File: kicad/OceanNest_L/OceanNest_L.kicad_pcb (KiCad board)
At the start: 2 copper layers, 104.5 x 86 mm, 38 parts, among them J1 MJ-4PP-9_BL_kai, SW1 SW_PUSH, SW10 SW_PUSH, SW11 SW_PUSH, SW12 SW_PUSH, SW13 SW_PUSH, SW14 SW_PUSH, SW15 SW_PUSH, SW16 SW_PUSH, SW2 SW_PUSH, SW3 SW_PUSH, SW4 SW_PUSH, SW5 SW_PUSH, SW6 SW_PUSH, SW7 SW_PUSH, SW8 SW_PUSH, SW9 SW_PUSH, U1 RP2040-Zero

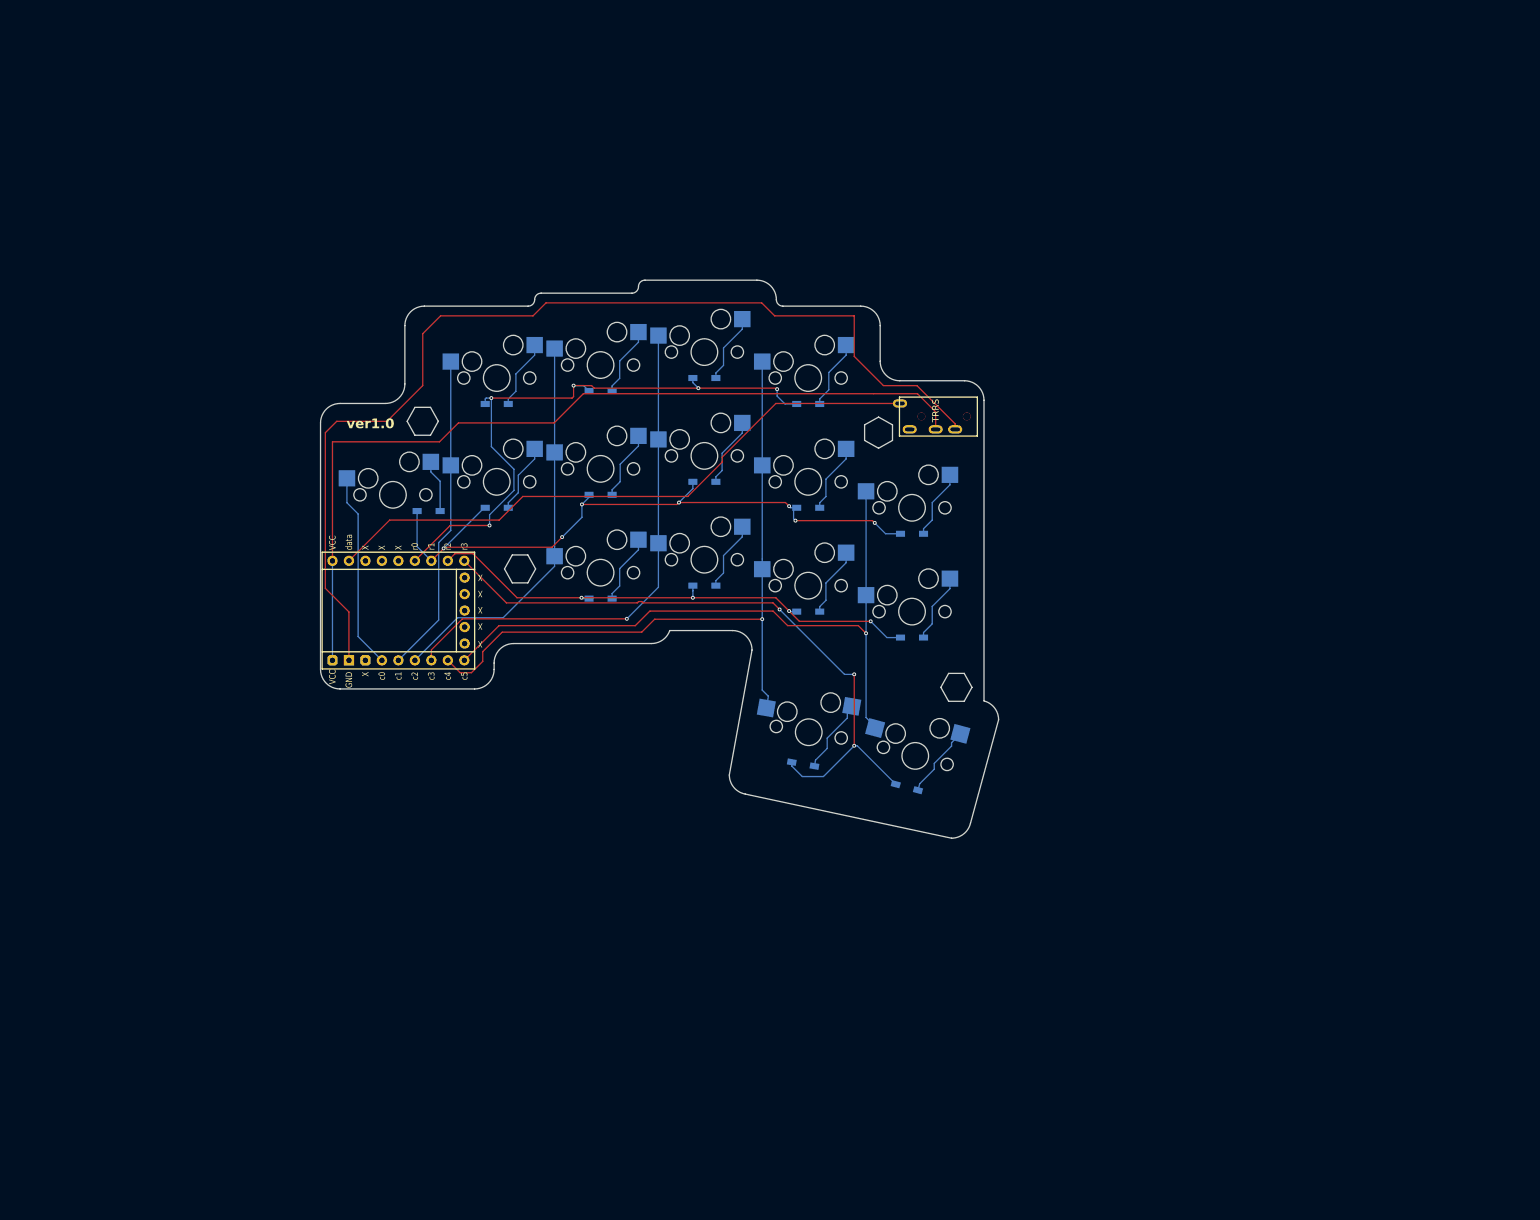
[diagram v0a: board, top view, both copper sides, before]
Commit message: feat: update PCB and schematic files for OceanNest project, including new components and layout adjustments
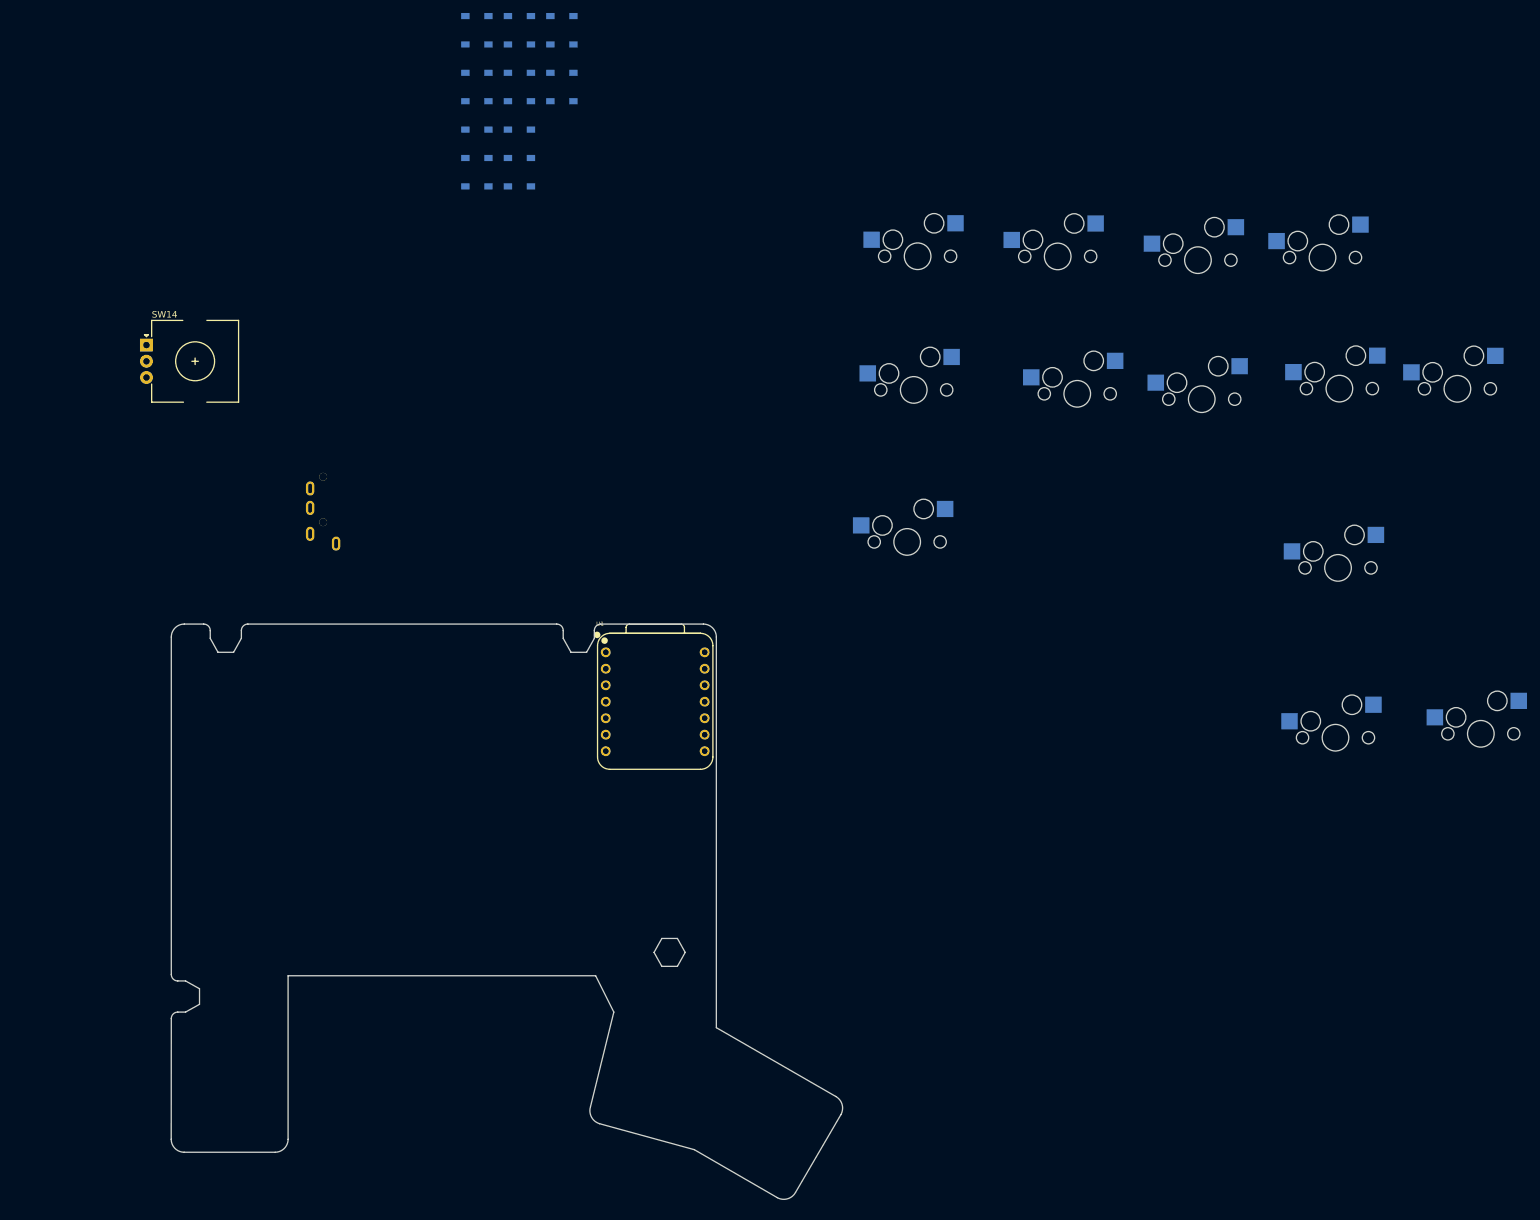
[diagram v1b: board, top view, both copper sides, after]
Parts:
- removed the Ref** at (181.0, 109.8)
- removed the Ref** at (169.0, 70.5)
- removed the Ref** at (113.8, 91.5)
- removed the Ref** at (98.8, 68.8)
- removed SW15, SW16: SW_PUSH, takashicompany:CherryMX_Hotswap_16m
- added D17: D, kbd_Parts:Diode_SMD, F.Cu at (120.2, 15.0)
- added D18: D, kbd_Parts:Diode_SMD, F.Cu at (120.2, 19.4)
- added Ref**: Val**, kbd_Hole:m2_Spacer_Hole_hex, F.Cu at (136.8, 150.6)
- D1, D10, D11, D12, D13, D14, D15, D16, D2, D3, D4, D5, D6, D7, D8, D9: footprint isw-kbd:Diode_SMD -> kbd_Parts:Diode_SMD
- J1: value MJ-4PP-9_BL_kai -> TRRS_MJ-4PP-9; moved to F.Cu
- SW1, SW10, SW11, SW12, SW13, SW2, SW3, SW4, SW5, SW6, SW7, SW8, SW9: value SW_PUSH -> SW_Push
- SW14: value SW_PUSH -> RotaryEncoder; footprint takashicompany:CherryMX_Hotswap_16m -> kbd_Parts:RotaryEncoder_Alps_EC12E_Vertical_H20mm
- U1: value RP2040-Zero -> XIAO-RP2040-DIP; footprint isw-kbd:RP2040-Zero -> xiao_rp2040:XIAO-RP2040-TH
- moved D16 126.2 mm to (120.2, 10.7), turned to 0 degrees
- moved SW14 124.9 mm to (56.2, 57.0)
- moved D15 121.1 mm to (120.2, 6.30), turned to 0 degrees
- moved SW11 113.7 mm to (239.8, 91.3)
- moved SW13 106.1 mm to (261.8, 116.9)
- moved SW9 101.1 mm to (258.2, 63.7)
- moved SW12 101.1 mm to (239.4, 117.5)
- moved SW8 98.4 mm to (240.0, 63.7)
- moved J1 95.7 mm to (83.4, 81.8), turned to 0 degrees
- moved D10 93.3 mm to (113.7, 15.0)
- moved SW7 93.3 mm to (218.8, 65.3)
- moved D14 92.2 mm to (113.7, 32.5)
- moved SW6 90.5 mm to (199.6, 64.5)
- moved D9 84.1 mm to (113.7, 10.7)
- moved D13 82.9 mm to (113.7, 28.2)
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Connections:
- D1 pad 1: row0 -> Net-(D1-K)
- D1 pad 2: Net-(D1-A) -> pin1
- D10 pad 1: row1 -> Net-(D10-K)
- D10 pad 2: Net-(D10-A) -> pin3
- D11 pad 1: row2 -> pin3
- D12 pad 1: row2 -> pin3
- D13 pad 1: row2 -> pin4
- D14 pad 1: row2 -> Net-(D14-K)
- D14 pad 2: Net-(D14-A) -> pin4
- D15 pad 1: row3 -> pin4
- D16 pad 1: row3 -> pin5
- D2 pad 1: row0 -> pin1
- D3 pad 1: row0 -> pin1
- D4 pad 1: row0 -> pin1
- D5 pad 1: row1 -> pin1
- D6 pad 1: row1 -> pin2
- D7 pad 1: row1 -> Net-(D7-K)
- D7 pad 2: Net-(D7-A) -> pin2
- D8 pad 1: row1 -> pin3
- D9 pad 1: row1 -> pin3
- SW1 pad 1: col1 -> Net-(D7-K)
- SW1 pad 2: Net-(D1-A) -> Net-(D2-A)
- SW10 pad 1: col5 -> Net-(D1-K)
- SW10 pad 2: Net-(D10-A) -> Net-(D13-A)
- SW11 pad 1: col2 -> Net-(D18-K)
- SW11 pad 2: Net-(D11-A) -> Net-(D15-A)
- SW12 pad 1: col3 -> Net-(D1-K)
- SW12 pad 2: Net-(D12-A) -> Net-(D16-A)
- SW13 pad 1: col4 -> Net-(D7-K)
- SW13 pad 2: Net-(D13-A) -> Net-(D17-A)
- SW2 pad 1: col2 -> Net-(D10-K)
- SW2 pad 2: Net-(D2-A) -> Net-(D3-A)
- SW3 pad 1: col3 -> Net-(D14-K)
- SW3 pad 2: Net-(D3-A) -> Net-(D4-A)
- SW4 pad 1: col4 -> Net-(D18-K)
- SW4 pad 2: Net-(D4-A) -> Net-(D5-A)
- SW5 pad 1: col0 -> Net-(D1-K)
- SW5 pad 2: Net-(D5-A) -> Net-(D6-A)
- SW6 pad 1: col1 -> Net-(D1-K)
- SW6 pad 2: Net-(D6-A) -> Net-(D8-A)
- SW7 pad 1: col2 -> Net-(D7-K)
- SW7 pad 2: Net-(D7-A) -> Net-(D9-A)
- SW8 pad 1: col3 -> Net-(D14-K)
- SW8 pad 2: Net-(D8-A) -> Net-(D11-A)
- SW9 pad 1: col4 -> Net-(D18-K)
- SW9 pad 2: Net-(D9-A) -> Net-(D12-A)
- U1 pad 1: data -> pin1
- U1 pad 10: unconnected-(U1-Pad10) -> REb
- U1 pad 11: unconnected-(U1-Pad11) -> REa
- U1 pad 13: unconnected-(U1-Pad13) -> GND
- U1 pad 14: col5 -> VCC
- U1 pad 2: unconnected-(U1-Pad2) -> pin2
- U1 pad 3: unconnected-(U1-Pad3) -> pin3
- U1 pad 4: unconnected-(U1-Pad4) -> pin4
- U1 pad 5: row0 -> pin5
- U1 pad 6: row1 -> data
- U1 pad 7: row2 -> VCC
- U1 pad 8: row3 -> unconnected-(U1-GPIO1/RX-Pad8)
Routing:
- net GND: track 158.9 -> 0.00 mm
- net VCC: track 133.6 -> 0.00 mm
- net col4: track 107.9 -> 0.00 mm, vias 1 -> 0
- net row1: track 104.3 -> 0.00 mm, vias 7 -> 0
- net col5: track 103.5 -> 0.00 mm, vias 1 -> 0
- net row3: track 100.2 -> 0.00 mm, vias 3 -> 0
- net data: track 95.4 -> 0.00 mm
- net row0: track 93.5 -> 0.00 mm, vias 5 -> 0
- net row2: track 79.9 -> 0.00 mm, vias 4 -> 0
- net col3: track 79.4 -> 0.00 mm, vias 1 -> 0
- net col2: track 61.1 -> 0.00 mm
- net col1: track 49.4 -> 0.00 mm
- net col0: track 30.3 -> 0.00 mm
- net Net-(D15-A): track 11.6 -> 0.00 mm
- net Net-(D16-A): track 11.3 -> 0.00 mm
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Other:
- board size 104.5 x 86 mm -> 103.5 x 88.7 mm
- board text removed: "ver1.0"

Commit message: feat: add new PCB and schematic files for OceanNest_L and OceanNest_L_Bottom, including layout adjustments and component updates
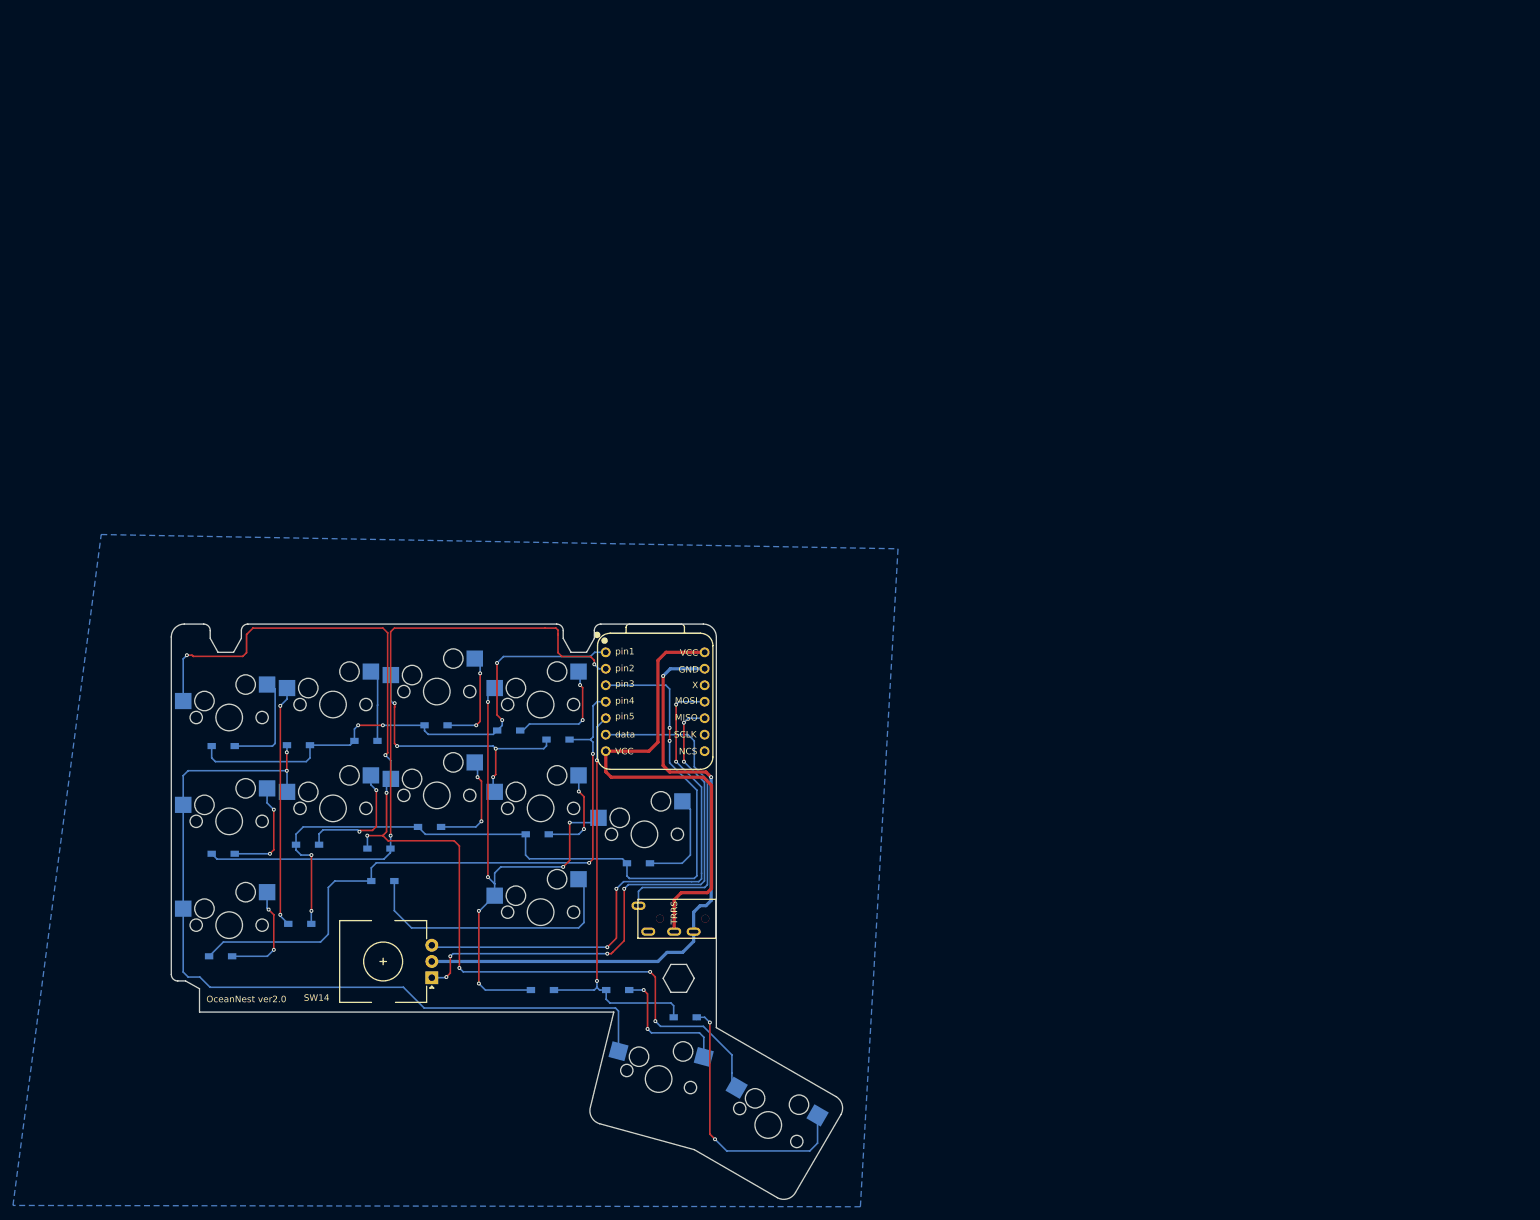
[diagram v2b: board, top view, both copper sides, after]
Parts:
- J1: moved to B.Cu
- moved D17 146.8 mm to (139.2, 160.6)
- moved D16 146.0 mm to (128.8, 156.4)
- moved SW9 142.9 mm to (132.9, 132.4)
- moved SW8 139.1 mm to (116.9, 128.4)
- moved SW4 138.8 mm to (116.9, 112.4)
- moved D18 137.0 mm to (117.2, 156.4)
- moved D15 136.1 mm to (92.6, 139.6)
- moved D10 135.5 mm to (79.8, 146.2)
- moved SW3 134.8 mm to (100.9, 110.4)
- moved SW11 133.9 mm to (116.9, 144.4)
- moved SW7 132.8 mm to (100.9, 126.4)
- moved D8 131.8 mm to (81.0, 134.0)
- moved D13 131.4 mm to (67.6, 151.2)
- moved SW2 131.3 mm to (84.9, 112.4)
- moved SW6 131.3 mm to (84.9, 128.4)
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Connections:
- U1 pad 10: REb -> REa
- U1 pad 11: REa -> REb
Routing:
- net Net-(D7-K): track 0.00 -> 166.9 mm, vias 0 -> 7
- net Net-(D1-K): track 0.00 -> 129.5 mm, vias 0 -> 2
- net pin3: track 0.00 -> 125.1 mm, vias 0 -> 4
- net pin2: track 0.00 -> 100.7 mm, vias 0 -> 2
- net pin4: track 0.00 -> 100.1 mm, vias 0 -> 2
- net GND: track 0.00 -> 97.4 mm, vias 0 -> 2
- net REa: track 0.00 -> 83.6 mm, vias 0 -> 6
- net REb: track 0.00 -> 83.6 mm, vias 0 -> 4
- net Net-(D18-K): track 0.00 -> 80.5 mm, vias 0 -> 6
- net pin1: track 0.00 -> 80.4 mm, vias 0 -> 4
- net VCC: track 0.00 -> 76.5 mm
- net pin5: track 0.00 -> 64.5 mm, vias 0 -> 2
- net data: track 0.00 -> 50.3 mm
- net Net-(D14-K): track 0.00 -> 42.8 mm, vias 0 -> 4
- net Net-(D17-A): track 0.00 -> 42.4 mm, vias 0 -> 2
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- added copper zone on B.Cu, net GND
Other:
- outline, holes or cut-outs redrawn
- board text added: "GND"
- board text added: "MISO"
- board text added: "MOSI"
- board text added: "NCS"
- board text added: "OceanNest ver2.0"
- board text added: "SCLK"
- board text added: "VCC"
- board text added: "X"
- board text added: "data"
- board text added: "pin1"
- board text added: "pin2"
- board text added: "pin3"
- board text added: "pin4"
- board text added: "pin5"
